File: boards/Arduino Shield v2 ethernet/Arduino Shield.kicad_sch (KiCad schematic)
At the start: 9 parts, among them U1 A000062, U2 W5500

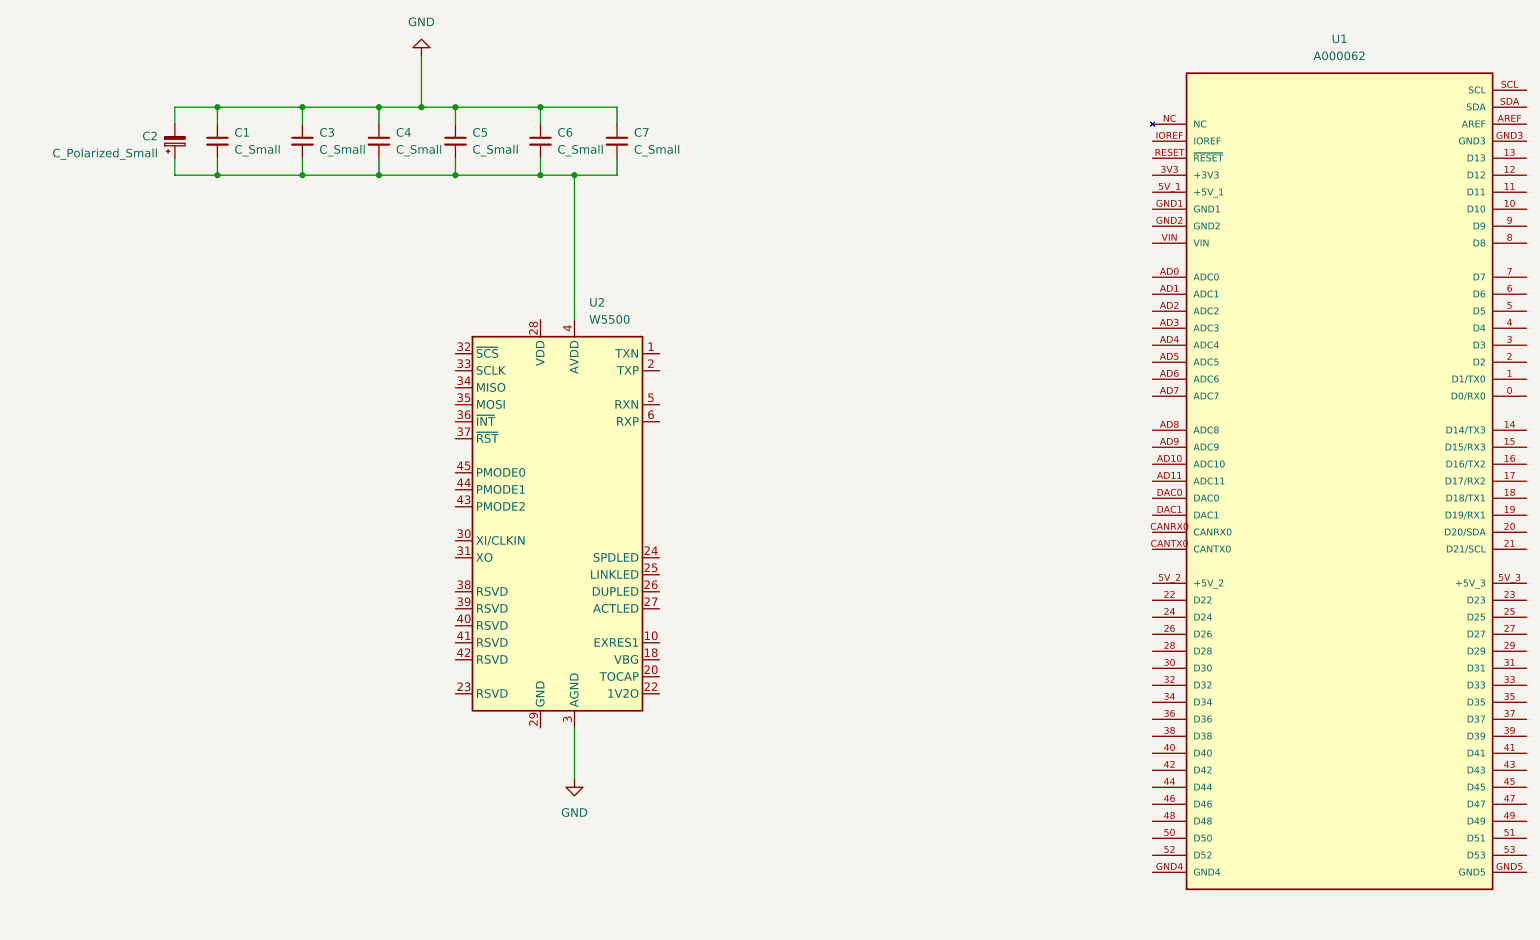
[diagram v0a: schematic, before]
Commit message: started shield v2 with ethernet
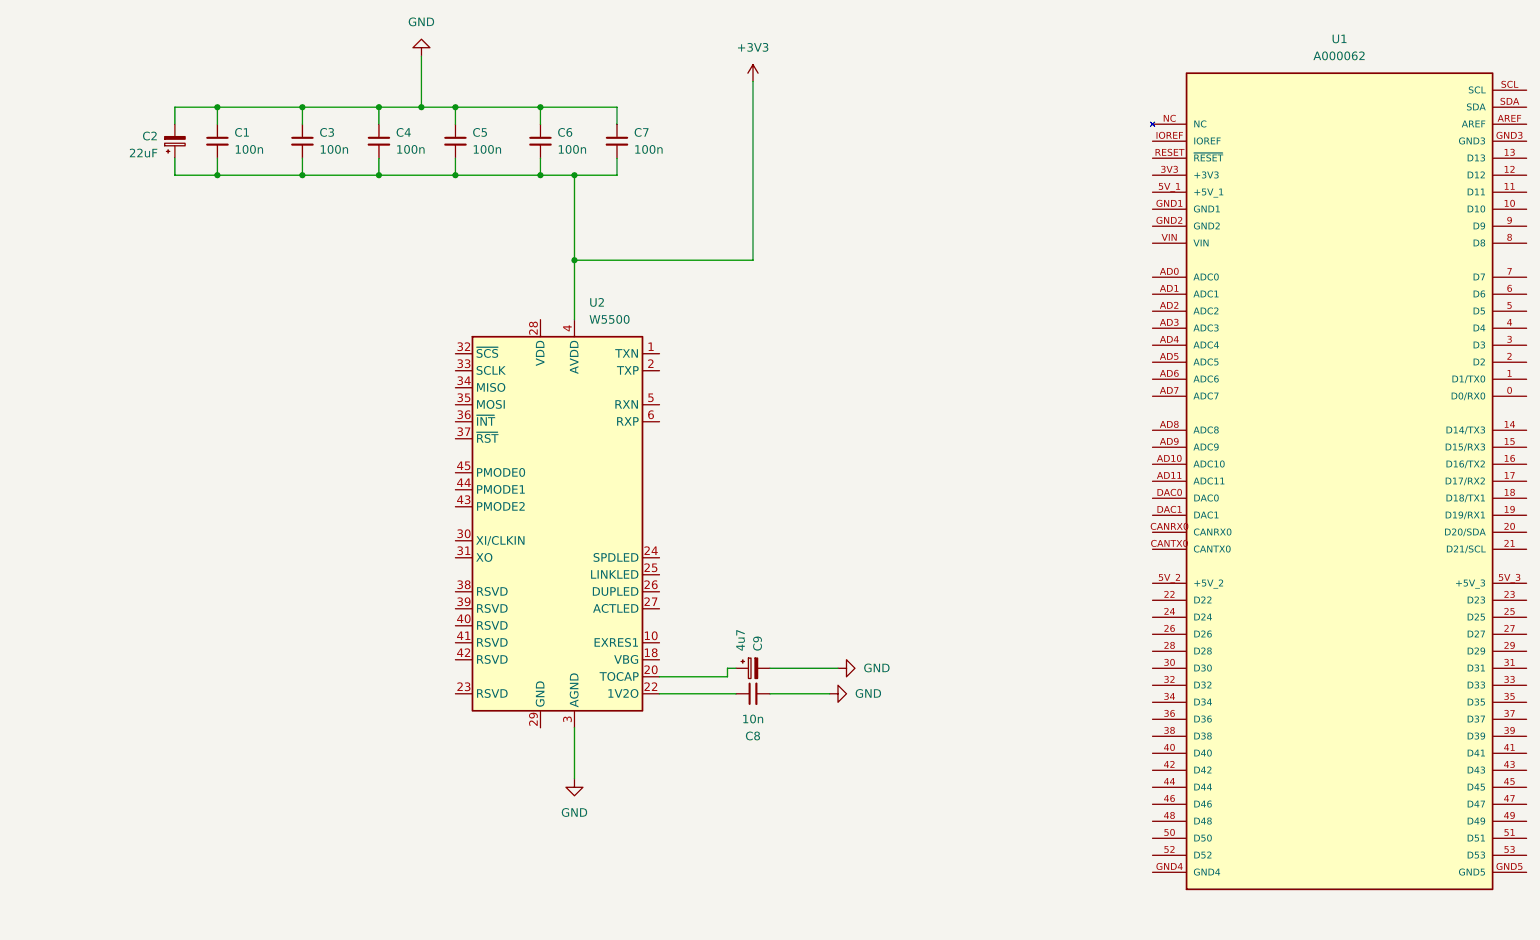
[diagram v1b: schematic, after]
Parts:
- added C8: 10n, symbol Device:C_Small
- added C9: 4u7, symbol Device:C_Polarized_Small
- C1, C3, C4, C5, C6, C7: value C_Small -> 100n
- C2: value C_Polarized_Small -> 22uF
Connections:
- net GND: now also C8.2, C9.2
- net +3V3: now reaches C1.2, C2.1, C3.2, C4.2, C5.2, C6.2, C7.2, U2.11 (AVDD), U2.15 (AVDD), U2.17 (AVDD), U2.21 (AVDD), U2.4 (AVDD), U2.8 (AVDD)
- net at U2.20 (TOCAP): now also C9.1
- net at U2.22 (1V2O): now also C8.1
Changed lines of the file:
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@@
   (junction (at 87.63 43.18) (diameter 0) (color 0 0 0 0)
   )
+  (junction (at 92.71 55.88) (diameter 0) (color 0 0 0 0)
+  )
   (junction (at 63.5 43.18) (diameter 0) (color 0 0 0 0)
   )
@@
     (stroke (width 0) (type default))
   )
-  (wire (pts (xy 92.71 43.18) (xy 92.71 64.77))
+  (wire (pts (xy 92.71 43.18) (xy 92.71 55.88))
     (stroke (width 0) (type default))
   )
@@
     (stroke (width 0) (type default))
   )
+  (wire (pts (xy 121.92 120.65) (xy 130.81 120.65))
+    (stroke (width 0) (type default))
+  )
   (wire (pts (xy 52.07 43.18) (xy 63.5 43.18))
     (stroke (width 0) (type default))
@@
     (stroke (width 0) (type default))
   )
+  (wire (pts (xy 92.71 55.88) (xy 92.71 64.77))
+    (stroke (width 0) (type default))
+  )
+  (wire (pts (xy 105.41 120.65) (xy 116.84 120.65))
+    (stroke (width 0) (type default))
+  )
   (wire (pts (xy 74.93 33.02) (xy 87.63 33.02))
     (stroke (width 0) (type default))
   )
+  (wire (pts (xy 115.57 118.11) (xy 115.57 116.84))
+    (stroke (width 0) (type default))
+  )
   (wire (pts (xy 33.02 43.18) (xy 39.37 43.18))
     (stroke (width 0) (type default))
@@
     (stroke (width 0) (type default))
   )
+  (wire (pts (xy 121.92 116.84) (xy 132.08 116.84))
+    (stroke (width 0) (type default))
+  )
   (wire (pts (xy 92.71 125.73) (xy 92.71 133.35))
     (stroke (width 0) (type default))
@@
     (stroke (width 0) (type default))
   )
+  (wire (pts (xy 119.38 55.88) (xy 92.71 55.88))
+    (stroke (width 0) (type default))
+  )
   (wire (pts (xy 39.37 43.18) (xy 52.07 43.18))
     (stroke (width 0) (type default))
@@
     (stroke (width 0) (type default))
   )
+  (wire (pts (xy 119.38 29.21) (xy 119.38 55.88))
+    (stroke (width 0) (type default))
+  )
   (wire (pts (xy 33.02 35.56) (xy 33.02 33.02))
     (stroke (width 0) (type default))
   )
   (wire (pts (xy 39.37 33.02) (xy 39.37 35.56))
+    (stroke (width 0) (type default))
+  )
+  (wire (pts (xy 105.41 118.11) (xy 115.57 118.11))
+    (stroke (width 0) (type default))
+  )
+  (wire (pts (xy 115.57 116.84) (xy 116.84 116.84))
     (stroke (width 0) (type default))
   )
@@
       (effects (font (size 1.27 1.27)) (justify right))
     )
-    (property "Value" "C_Polarized_Small" (at 30.48 39.9161 0)
+    (property "Value" "22uF" (at 30.48 39.9161 0)
       (effects (font (size 1.27 1.27)) (justify right))
     )
@@
     )
   )
+  (symbol (lib_id "Device:C_Small") (at 119.38 120.65 90) (mirror x) (unit 1)
+    (in_bom yes) (on_board yes) (dnp no)
+    (property "Reference" "C8" (at 119.3863 127 90)
+      (effects (font (size 1.27 1.27)))
+    )
+    (property "Value" "10n" (at 119.3863 124.46 90)
+      (effects (font (size 1.27 1.27)))
+    )
+    (property "Footprint" "" (at 119.38 120.65 0)
+      (effects (font (size 1.27 1.27)) hide)
+    )
+    (property "Datasheet" "~" (at 119.38 120.65 0)
+      (effects (font (size 1.27 1.27)) hide)
+    )
+    (pin "1")
+    (pin "2")
+    (instances
+      (project "Arduino Shield"
+        (path "/d32bdb2e-fa3a-461a-9e34-c0053c91b5d5"
+          (reference "C8") (unit 1)
+        )
+      )
+    )
+  )
   (symbol (lib_id "Device:C_Small") (at 99.06 38.1 0) (unit 1)
     (in_bom yes) (on_board yes) (dnp no) (fields_autoplaced)
@@
       (effects (font (size 1.27 1.27)) (justify left))
     )
-    (property "Value" "C_Small" (at 101.6 39.3763 0)
+    (property "Value" "100n" (at 101.6 39.3763 0)
       (effects (font (size 1.27 1.27)) (justify left))
     )
@@
     )
   )
+  (symbol (lib_id "power:GND") (at 132.08 116.84 90) (unit 1)
+    (in_bom yes) (on_board yes) (dnp no) (fields_autoplaced)
+    (property "Reference" "#PWR05" (at 138.43 116.84 0)
+      (effects (font (size 1.27 1.27)) hide)
+    )
+    (property "Value" "GND" (at 135.89 116.84 90)
+      (effects (font (size 1.27 1.27)) (justify right))
+    )
+    (property "Footprint" "" (at 132.08 116.84 0)
+      (effects (font (size 1.27 1.27)) hide)
+    )
+    (property "Datasheet" "" (at 132.08 116.84 0)
+      (effects (font (size 1.27 1.27)) hide)
+    )
+    (pin "1")
+    (instances
+      (project "Arduino Shield"
+        (path "/d32bdb2e-fa3a-461a-9e34-c0053c91b5d5"
+          (reference "#PWR05") (unit 1)
+        )
+      )
+    )
+  )
   (symbol (lib_id "Device:C_Small") (at 87.63 38.1 0) (unit 1)
     (in_bom yes) (on_board yes) (dnp no) (fields_autoplaced)
@@
       (effects (font (size 1.27 1.27)) (justify left))
     )
-    (property "Value" "C_Small" (at 90.17 39.3763 0)
+    (property "Value" "100n" (at 90.17 39.3763 0)
       (effects (font (size 1.27 1.27)) (justify left))
     )
@@
       (effects (font (size 1.27 1.27)) (justify left))
     )
-    (property "Value" "C_Small" (at 77.47 39.3763 0)
+    (property "Value" "100n" (at 77.47 39.3763 0)
       (effects (font (size 1.27 1.27)) (justify left))
     )
@@
       (effects (font (size 1.27 1.27)) (justify left))
     )
-    (property "Value" "C_Small" (at 41.91 39.3763 0)
+    (property "Value" "100n" (at 41.91 39.3763 0)
       (effects (font (size 1.27 1.27)) (justify left))
     )
@@
     )
   )
+  (symbol (lib_id "Device:C_Polarized_Small") (at 119.38 116.84 90) (mirror x) (unit 1)
+    (in_bom yes) (on_board yes) (dnp no)
+    (property "Reference" "C9" (at 120.1039 114.3 0)
+      (effects (font (size 1.27 1.27)) (justify right))
+    )
+    (property "Value" "4u7" (at 117.5639 114.3 0)
+      (effects (font (size 1.27 1.27)) (justify right))
+    )
+    (property "Footprint" "" (at 119.38 116.84 0)
+      (effects (font (size 1.27 1.27)) hide)
+    )
+    (property "Datasheet" "~" (at 119.38 116.84 0)
+      (effects (font (size 1.27 1.27)) hide)
+    )
+    (pin "1")
+    (pin "2")
+    (instances
+      (project "Arduino Shield"
+        (path "/d32bdb2e-fa3a-461a-9e34-c0053c91b5d5"
+          (reference "C9") (unit 1)
+        )
+      )
+    )
+  )
+  (symbol (lib_id "power:GND") (at 130.81 120.65 90) (unit 1)
+    (in_bom yes) (on_board yes) (dnp no) (fields_autoplaced)
+    (property "Reference" "#PWR04" (at 137.16 120.65 0)
+      (effects (font (size 1.27 1.27)) hide)
+    )
+    (property "Value" "GND" (at 134.62 120.65 90)
+      (effects (font (size 1.27 1.27)) (justify right))
+    )
+    (property "Footprint" "" (at 130.81 120.65 0)
+      (effects (font (size 1.27 1.27)) hide)
+    )
+    (property "Datasheet" "" (at 130.81 120.65 0)
+      (effects (font (size 1.27 1.27)) hide)
+    )
+    (pin "1")
+    (instances
+      (project "Arduino Shield"
+        (path "/d32bdb2e-fa3a-461a-9e34-c0053c91b5d5"
+          (reference "#PWR04") (unit 1)
+        )
+      )
+    )
+  )
   (symbol (lib_id "Device:C_Small") (at 52.07 38.1 0) (unit 1)
     (in_bom yes) (on_board yes) (dnp no) (fields_autoplaced)
@@
       (effects (font (size 1.27 1.27)) (justify left))
     )
-    (property "Value" "C_Small" (at 54.61 39.3763 0)
+    (property "Value" "100n" (at 54.61 39.3763 0)
       (effects (font (size 1.27 1.27)) (justify left))
     )
@@
     )
   )
+  (symbol (lib_id "power:+3V3") (at 119.38 29.21 0) (unit 1)
+    (in_bom yes) (on_board yes) (dnp no) (fields_autoplaced)
+    (property "Reference" "#PWR03" (at 119.38 33.02 0)
+      (effects (font (size 1.27 1.27)) hide)
+    )
+    (property "Value" "+3V3" (at 119.38 24.13 0)
+      (effects (font (size 1.27 1.27)))
+    )
+    (property "Footprint" "" (at 119.38 29.21 0)
+      (effects (font (size 1.27 1.27)) hide)
+    )
+    (property "Datasheet" "" (at 119.38 29.21 0)
+      (effects (font (size 1.27 1.27)) hide)
+    )
+    (pin "1")
+    (instances
+      (project "Arduino Shield"
+        (path "/d32bdb2e-fa3a-461a-9e34-c0053c91b5d5"
+          (reference "#PWR03") (unit 1)
+        )
+      )
+    )
+  )
   (symbol (lib_id "Device:C_Small") (at 63.5 38.1 0) (unit 1)
     (in_bom yes) (on_board yes) (dnp no) (fields_autoplaced)
@@
       (effects (font (size 1.27 1.27)) (justify left))
     )
-    (property "Value" "C_Small" (at 66.04 39.3763 0)
-      (effects (font (size 1.27 1.27)) (justify left))
-    )
+    (property "Value" "100n" (at 66.04 39.3763 0)
+      (effects (font (size 1.27 1.27)) (justify left))
+    )
